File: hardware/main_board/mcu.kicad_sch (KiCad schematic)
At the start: 9 parts, among them SW2 SW_Push, U4 STM32G0B1CBTx

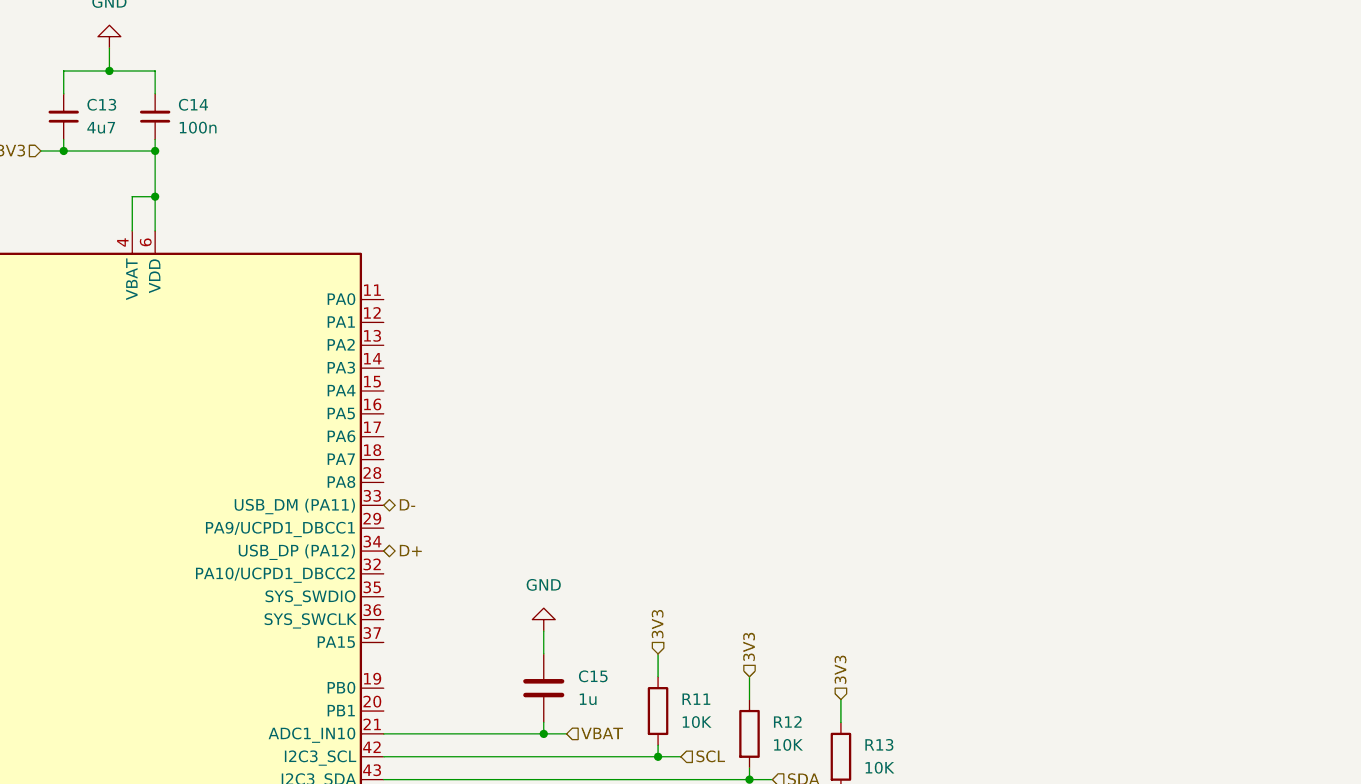
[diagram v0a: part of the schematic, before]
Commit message: Add probe connector
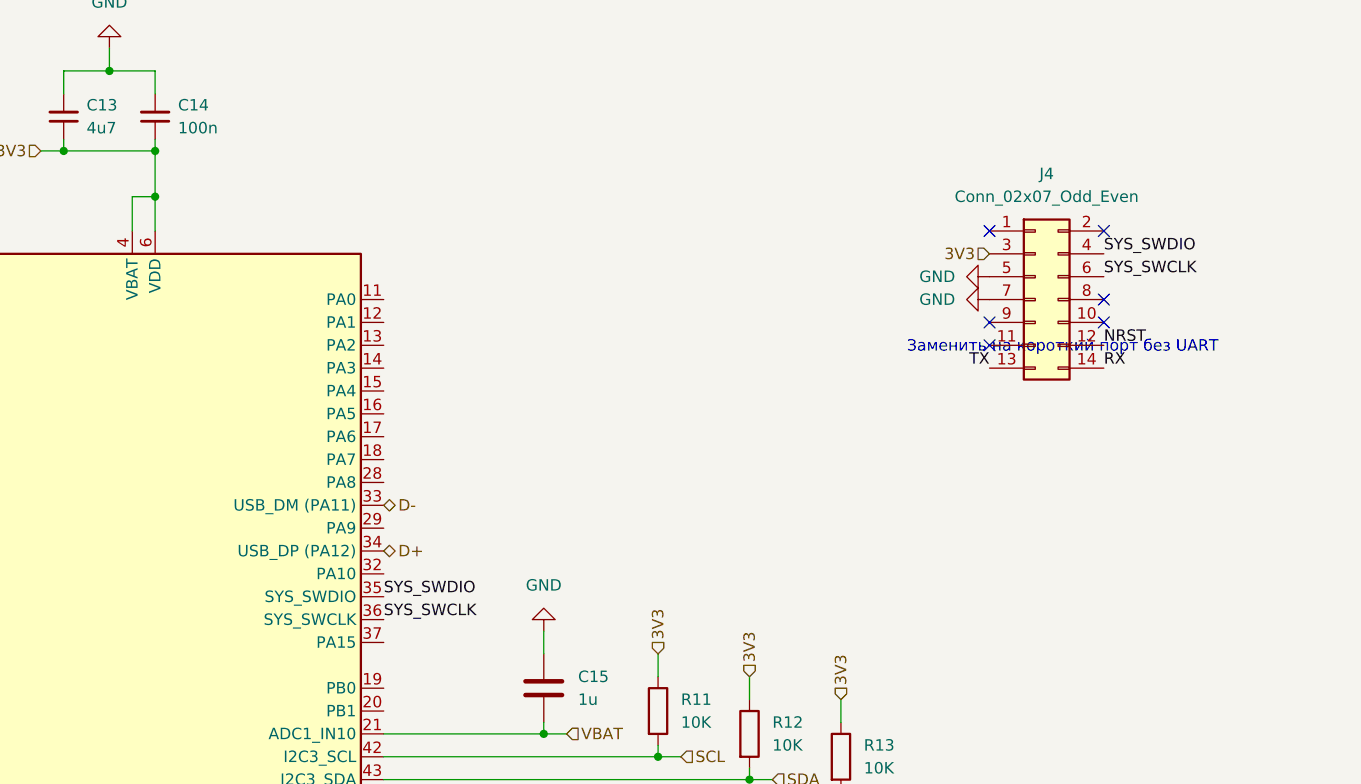
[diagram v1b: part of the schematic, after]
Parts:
- added J4: Conn_02x07_Odd_Even, Project_Footprints:SAMTEC_FTSH-107-01-L-DV-K-A, symbol Connector_Generic:Conn_02x07_Odd_Even
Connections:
- net 3V3: now also J4.3 (Pin_3)
- net GND: now also J4.5 (Pin_5), J4.7 (Pin_7)
- net NRST: now also J4.12 (Pin_12)
- net SYS_SWDIO: now reaches U4.35 (PA13)
- net SYS_SWDIO: now also J4.4 (Pin_4)
- net SYS_SWCLK: now reaches U4.36 (PA14)
- net SYS_SWCLK: now also J4.6 (Pin_6)
- new net RX: J4.14 (Pin_14)
- new net TX: J4.13 (Pin_13)
- no-connect marks 0 -> 6
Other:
- note added: "Заменить на короткий порт без UART"

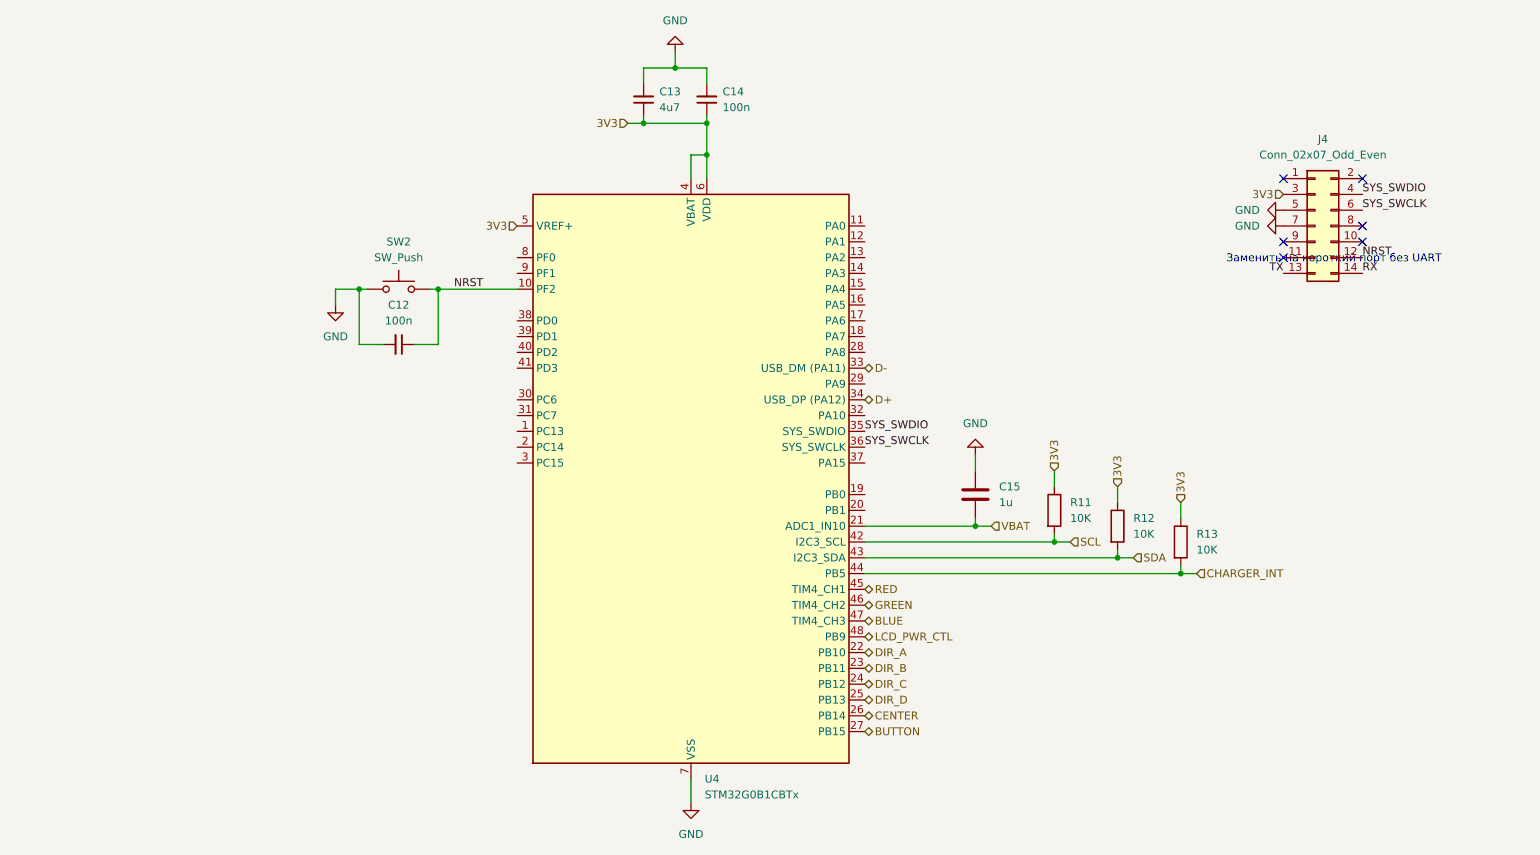
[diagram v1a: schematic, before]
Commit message: Add daughter board connector
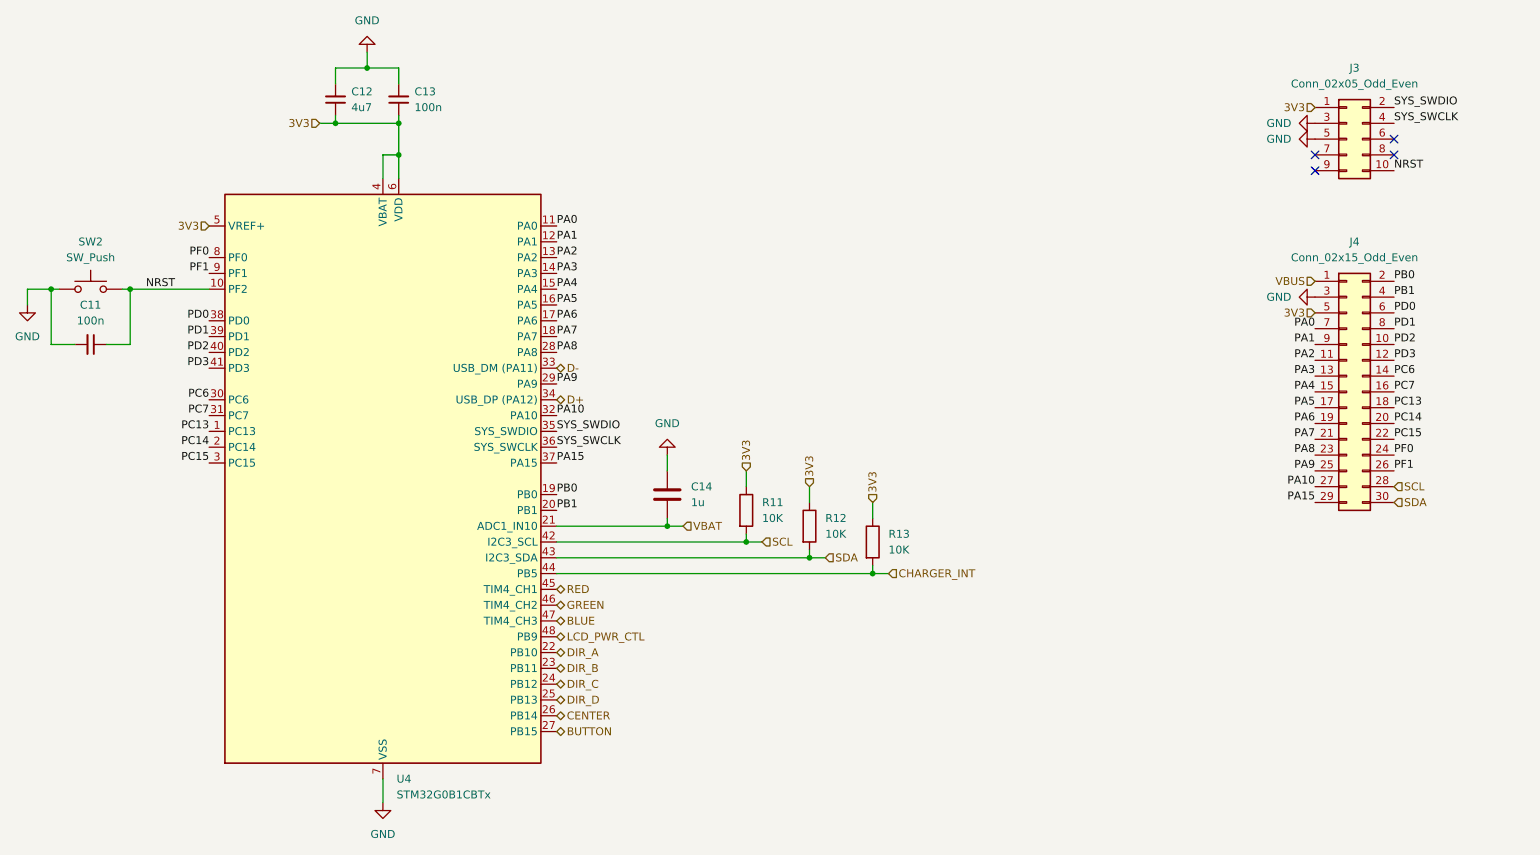
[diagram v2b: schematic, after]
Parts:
- removed J4: Conn_02x07_Odd_Even, Project_Footprints:SAMTEC_FTSH-107-01-L-DV-K-A, symbol Connector_Generic:Conn_02x07_Odd_Even
- added J3: Conn_02x05_Odd_Even, Project_Footprints:SAMTEC_FTSH-105-XX-X-DV, symbol Connector_Generic:Conn_02x05_Odd_Even
- added J4: Conn_02x15_Odd_Even, symbol Connector_Generic:Conn_02x15_Odd_Even
- renumbered C12 to C11, C13 to C12, C14 to C13, C15 to C14
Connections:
- net 3V3: now also J3.1 (Pin_1), J4.5 (Pin_5)
- net GND: now also J3.3 (Pin_3), J3.5 (Pin_5), J4.3 (Pin_3)
- net NRST: now also J3.10 (Pin_10)
- net SCL: now also J4.28 (Pin_28)
- net SDA: now also J4.30 (Pin_30)
- net SYS_SWCLK: now also J3.4 (Pin_4)
- net SYS_SWDIO: now also J3.2 (Pin_2)
- net PC13: now reaches U4.1 (PC13)
- net PC13: now also J4.18 (Pin_18)
- net PA0: now reaches U4.11 (PA0)
- net PA0: now also J4.7 (Pin_7)
- net PA1: now reaches U4.12 (PA1)
- net PA1: now also J4.9 (Pin_9)
- net PA2: now reaches U4.13 (PA2)
- net PA2: now also J4.11 (Pin_11)
- net PA3: now reaches U4.14 (PA3)
- net PA3: now also J4.13 (Pin_13)
- net PA4: now reaches U4.15 (PA4)
- net PA4: now also J4.15 (Pin_15)
- net PA5: now reaches U4.16 (PA5)
- net PA5: now also J4.17 (Pin_17)
- net PA6: now reaches U4.17 (PA6)
- net PA6: now also J4.19 (Pin_19)
- net PA7: now reaches U4.18 (PA7)
- net PA7: now also J4.21 (Pin_21)
- net PB0: now reaches U4.19 (PB0)
- net PB0: now also J4.2 (Pin_2)
- net PC14: now reaches U4.2 (PC14)
- net PC14: now also J4.20 (Pin_20)
- net PB1: now reaches U4.20 (PB1)
- net PB1: now also J4.4 (Pin_4)
- net PA8: now reaches U4.28 (PA8)
- net PA8: now also J4.23 (Pin_23)
- net PA9: now reaches U4.29 (PA9/UCPD1_DBCC1)
- net PA9: now also J4.25 (Pin_25)
- net PC15: now reaches U4.3 (PC15)
- net PC15: now also J4.22 (Pin_22)
- net PC6: now reaches U4.30 (PC6)
- net PC6: now also J4.14 (Pin_14)
- net PC7: now reaches U4.31 (PC7)
- net PC7: now also J4.16 (Pin_16)
- net PA10: now reaches U4.32 (PA10/UCPD1_DBCC2)
- net PA10: now also J4.27 (Pin_27)
- net PA15: now reaches U4.37 (PA15)
- net PA15: now also J4.29 (Pin_29)
- net PD0: now reaches U4.38 (PD0)
- net PD0: now also J4.6 (Pin_6)
- net PD1: now reaches U4.39 (PD1)
- net PD1: now also J4.8 (Pin_8)
- net PD2: now reaches U4.40 (PD2)
- net PD2: now also J4.10 (Pin_10)
- net PD3: now reaches U4.41 (PD3)
- net PD3: now also J4.12 (Pin_12)
- net PF0: now reaches U4.8 (PF0)
- net PF0: now also J4.24 (Pin_24)
- net PF1: now reaches U4.9 (PF1)
- net PF1: now also J4.26 (Pin_26)
- new net VBUS: J4.1 (Pin_1)
- no-connect marks 6 -> 4
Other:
- note removed: "Заменить на короткий порт без UART"
- moved on the sheet: C11, C12, C13, C14, R11, R12, R13, SW2, U4

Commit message: Board schematic complete
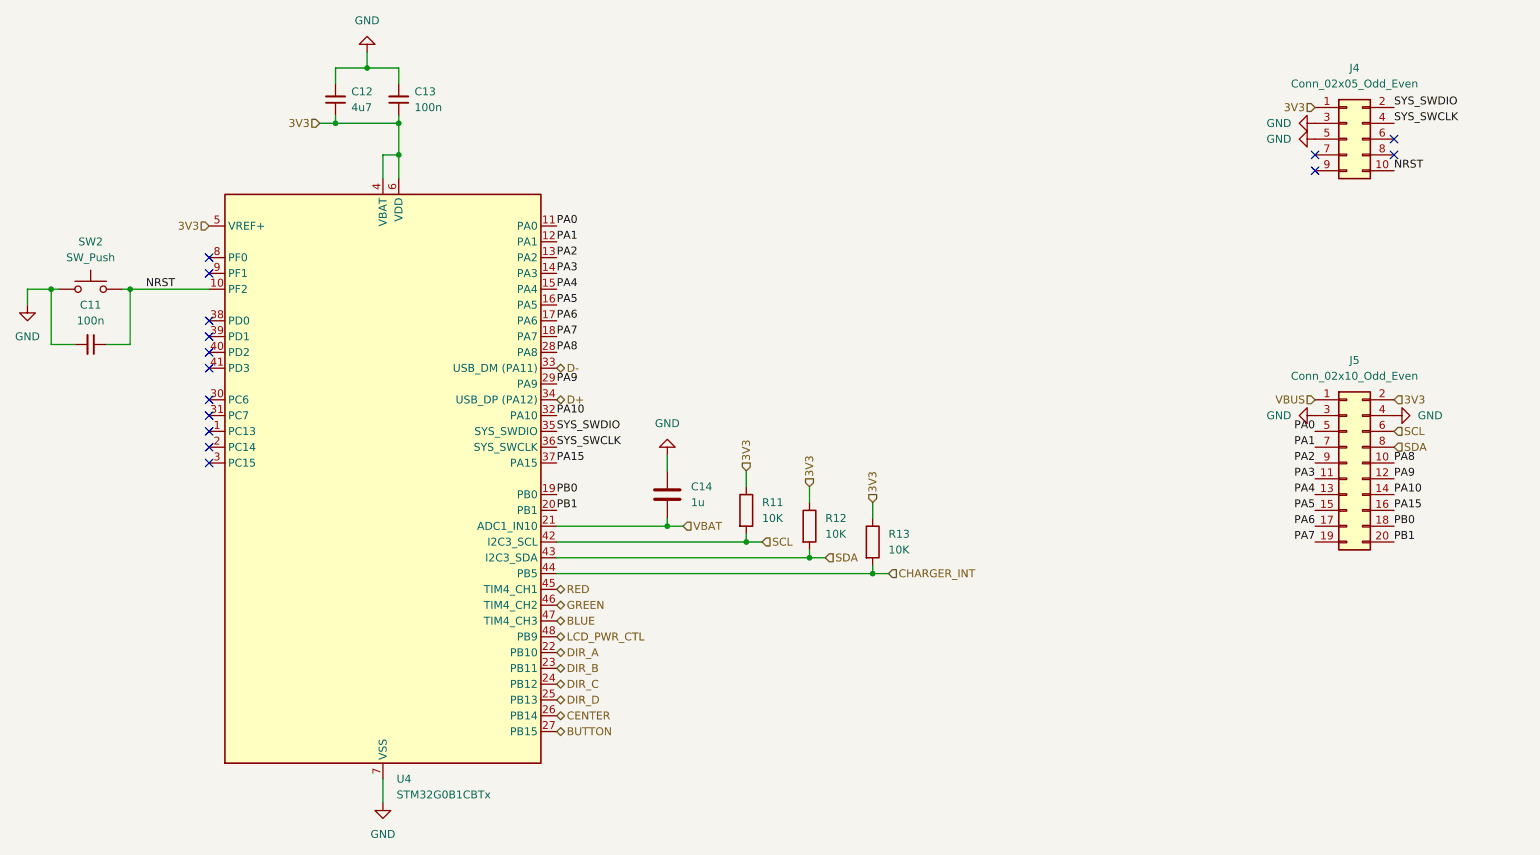
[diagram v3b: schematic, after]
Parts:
- removed J4: Conn_02x15_Odd_Even, symbol Connector_Generic:Conn_02x15_Odd_Even
- added J5: Conn_02x10_Odd_Even, symbol Connector_Generic:Conn_02x10_Odd_Even
- renumbered J3 to J4
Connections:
- net 3V3: now also J5.2 (Pin_2)
- net GND: now also J5.3 (Pin_3), J5.4 (Pin_4)
- net PA0: now also J5.5 (Pin_5)
- net PA1: now also J5.7 (Pin_7)
- net PA10: now also J5.14 (Pin_14)
- net PA15: now also J5.16 (Pin_16)
- net PA2: now also J5.9 (Pin_9)
- net PA3: now also J5.11 (Pin_11)
- net PA4: now also J5.13 (Pin_13)
- net PA5: now also J5.15 (Pin_15)
- net PA6: now also J5.17 (Pin_17)
- net PA7: now also J5.19 (Pin_19)
- net PA8: now also J5.10 (Pin_10)
- net PA9: now also J5.12 (Pin_12)
- net PB0: now also J5.18 (Pin_18)
- net PB1: now also J5.20 (Pin_20)
- net SCL: now also J5.6 (Pin_6)
- net SDA: now also J5.8 (Pin_8)
- net VBUS: now also J5.1 (Pin_1)
- net PC13: no longer names the net of U4.1 (PC13)
- net PC14: no longer names the net of U4.2 (PC14)
- net PC15: no longer names the net of U4.3 (PC15)
- net PC6: no longer names the net of U4.30 (PC6)
- net PC7: no longer names the net of U4.31 (PC7)
- net PD0: no longer names the net of U4.38 (PD0)
- net PD1: no longer names the net of U4.39 (PD1)
- net PD2: no longer names the net of U4.40 (PD2)
- net PD3: no longer names the net of U4.41 (PD3)
- net PF0: no longer names the net of U4.8 (PF0)
- net PF1: no longer names the net of U4.9 (PF1)
- no-connect marks 4 -> 15
